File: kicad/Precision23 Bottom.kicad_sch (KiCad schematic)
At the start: 12 parts, among them J396 STANDOFF, J397 STANDOFF, J398 STANDOFF, J399 STANDOFF, J504 Conn_01x06, J507 Conn_01x06, J508 Conn_01x06, J509 Conn_01x02_Pin, J895 USB A Male to Blank

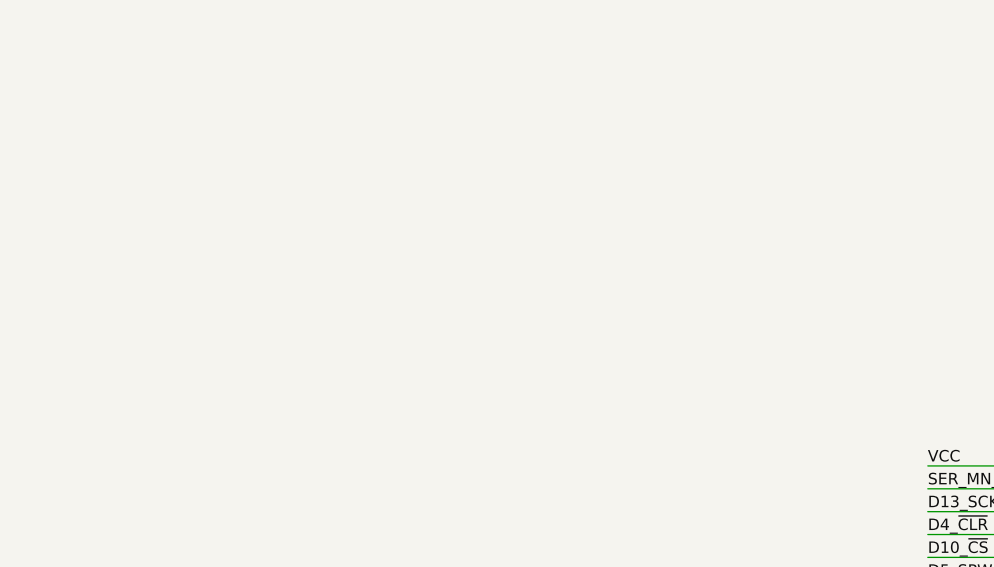
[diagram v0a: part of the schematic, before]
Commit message: Added top and bottom schematics to support refactor of board
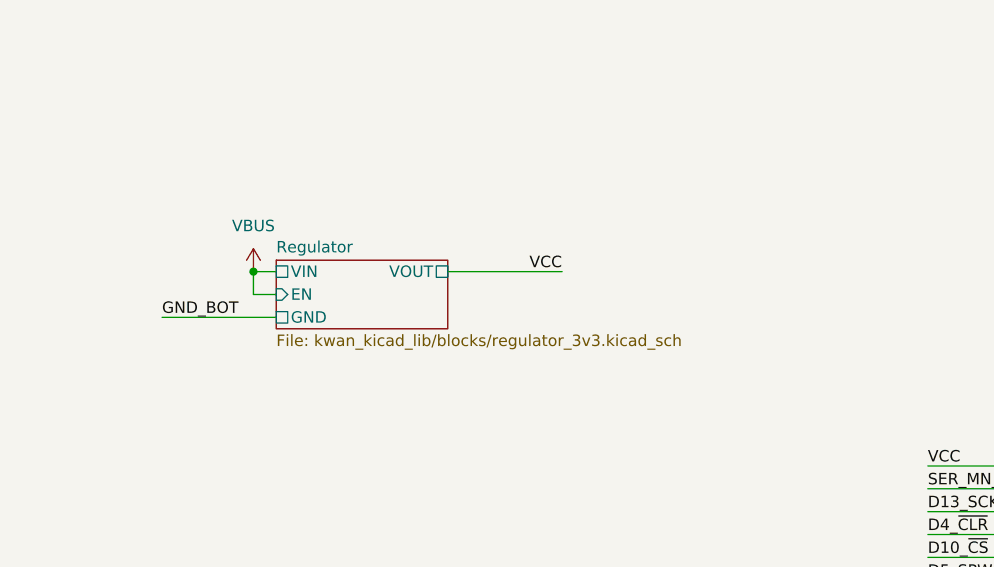
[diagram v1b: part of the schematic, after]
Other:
- added sheet Regulator (kwan_kicad_lib/blocks/regulator_3v3.kicad_sch)
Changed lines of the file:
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@@
   (junction (at 46.99 181.61) (diameter 0) (color 0 0 0 0)
+  )
+  (junction (at 102.87 78.74) (diameter 0) (color 0 0 0 0)
   )
   (junction (at 46.99 179.07) (diameter 0) (color 0 0 0 0)
@@
     (stroke (width 0) (type default))
   )
+  (wire (pts (xy 124.46 78.74) (xy 137.16 78.74))
+    (stroke (width 0) (type default))
+  )
   (wire (pts (xy 46.99 168.91) (xy 57.15 168.91))
     (stroke (width 0) (type default))
@@
     (stroke (width 0) (type default))
   )
+  (wire (pts (xy 105.41 81.28) (xy 102.87 81.28))
+    (stroke (width 0) (type default))
+  )
   (wire (pts (xy 46.99 176.53) (xy 57.15 176.53))
     (stroke (width 0) (type default))
@@
     (stroke (width 0) (type default))
   )
+  (wire (pts (xy 92.71 83.82) (xy 105.41 83.82))
+    (stroke (width 0) (type default))
+  )
   (wire (pts (xy 40.64 41.91) (xy 54.61 41.91))
     (stroke (width 0) (type default))
   )
+  (wire (pts (xy 102.87 78.74) (xy 105.41 78.74))
+    (stroke (width 0) (type default))
+  )
   (wire (pts (xy 34.29 179.07) (xy 46.99 179.07))
     (stroke (width 0) (type default))
@@
   )
   (wire (pts (xy 177.8 127) (xy 190.5 127))
+    (stroke (width 0) (type default))
+  )
+  (wire (pts (xy 102.87 81.28) (xy 102.87 78.74))
     (stroke (width 0) (type default))
   )
@@
     (effects (font (size 1.27 1.27)) (justify left bottom))
   )
+  (label "GND_BOT" (at 92.71 83.82 0) (fields_autoplaced)
+    (effects (font (size 1.27 1.27)) (justify left bottom))
+  )
   (label "GND_BOT" (at 50.8 114.3 180) (fields_autoplaced)
+    (effects (font (size 1.27 1.27)) (justify right bottom))
+  )
+  (label "VCC" (at 137.16 78.74 180) (fields_autoplaced)
     (effects (font (size 1.27 1.27)) (justify right bottom))
   )
@@
     )
   )
+  (symbol (lib_id "power:VBUS") (at 102.87 78.74 0) (unit 1)
+    (in_bom yes) (on_board yes) (dnp no) (fields_autoplaced)
+    (property "Reference" "#PWR0310" (at 102.87 82.55 0)
+      (effects (font (size 1.27 1.27)) hide)
+    )
+    (property "Value" "VBUS" (at 102.87 73.66 0)
+      (effects (font (size 1.27 1.27)))
+    )
+    (property "Footprint" "" (at 102.87 78.74 0)
+      (effects (font (size 1.27 1.27)) hide)
+    )
+    (property "Datasheet" "" (at 102.87 78.74 0)
+      (effects (font (size 1.27 1.27)) hide)
+    )
+    (pin "1")
+    (instances
+      (project "Precision23"
+        (path "/9151f981-b383-4946-8df4-92ef46ef2206"
+          (reference "#PWR0310") (unit 1)
+        )
+        (path "/9151f981-b383-4946-8df4-92ef46ef2206/b9b5a9b9-9a45-4bb4-8a5d-f3809553447a"
+          (reference "#PWR0303") (unit 1)
+        )
+        (path "/9151f981-b383-4946-8df4-92ef46ef2206/9f66be35-2744-413f-8b31-a996047a434b"
+          (reference "#PWR0303") (unit 1)
+        )
+      )
+    )
+  )
   (symbol (lib_id "Connector_Generic:Conn_01x06") (at 59.69 39.37 0) (unit 1)
     (in_bom yes) (on_board yes) (dnp no)
@@
       )
     )
+  )
+  (sheet (at 105.41 77.47) (size 19.05 7.62) (fields_autoplaced)
+    (stroke (width 0.1524) (type solid))
+    (fill (color 0 0 0 0.0000))
+    (property "Sheetname" "Regulator" (at 105.41 76.7584 0)
+      (effects (font (size 1.27 1.27)) (justify left bottom))
+    )
+    (property "Sheetfile" "kwan_kicad_lib/blocks/regulator_3v3.kicad_sch" (at 105.41 85.6746 0)
+      (effects (font (size 1.27 1.27)) (justify left top))
+    )
+    (pin "GND" passive (at 105.41 83.82 180)
+      (effects (font (size 1.27 1.27)) (justify left))
+    )
+    (pin "VIN" passive (at 105.41 78.74 180)
+      (effects (font (size 1.27 1.27)) (justify left))
+    )
+    (pin "EN" input (at 105.41 81.28 180)
+      (effects (font (size 1.27 1.27)) (justify left))
+    )
+    (pin "VOUT" passive (at 124.46 78.74 0)
+      (effects (font (size 1.27 1.27)) (justify right))
+    )
+    (instances
+      (project "Precision23"
+        (path "/9151f981-b383-4946-8df4-92ef46ef2206" (page "6"))
+        (path "/9151f981-b383-4946-8df4-92ef46ef2206/b9b5a9b9-9a45-4bb4-8a5d-f3809553447a" (page "6"))
+        (path "/9151f981-b383-4946-8df4-92ef46ef2206/9f66be35-2744-413f-8b31-a996047a434b" (page "6"))
+      )
+    )

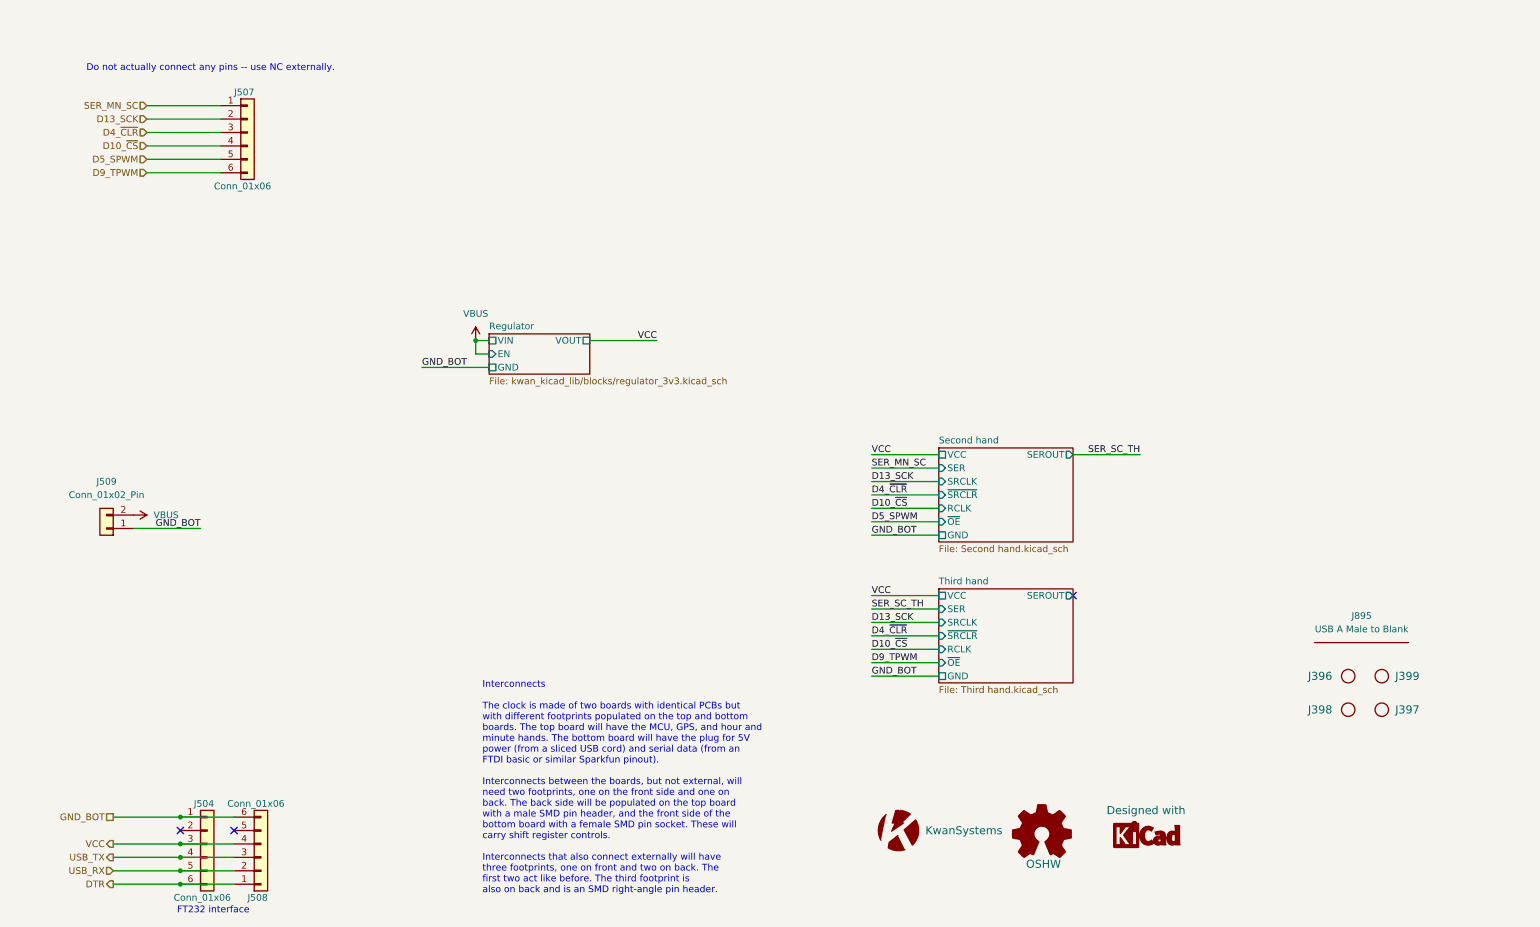
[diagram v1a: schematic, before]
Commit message: Refactored board, put 5V0 on all parts except GPS
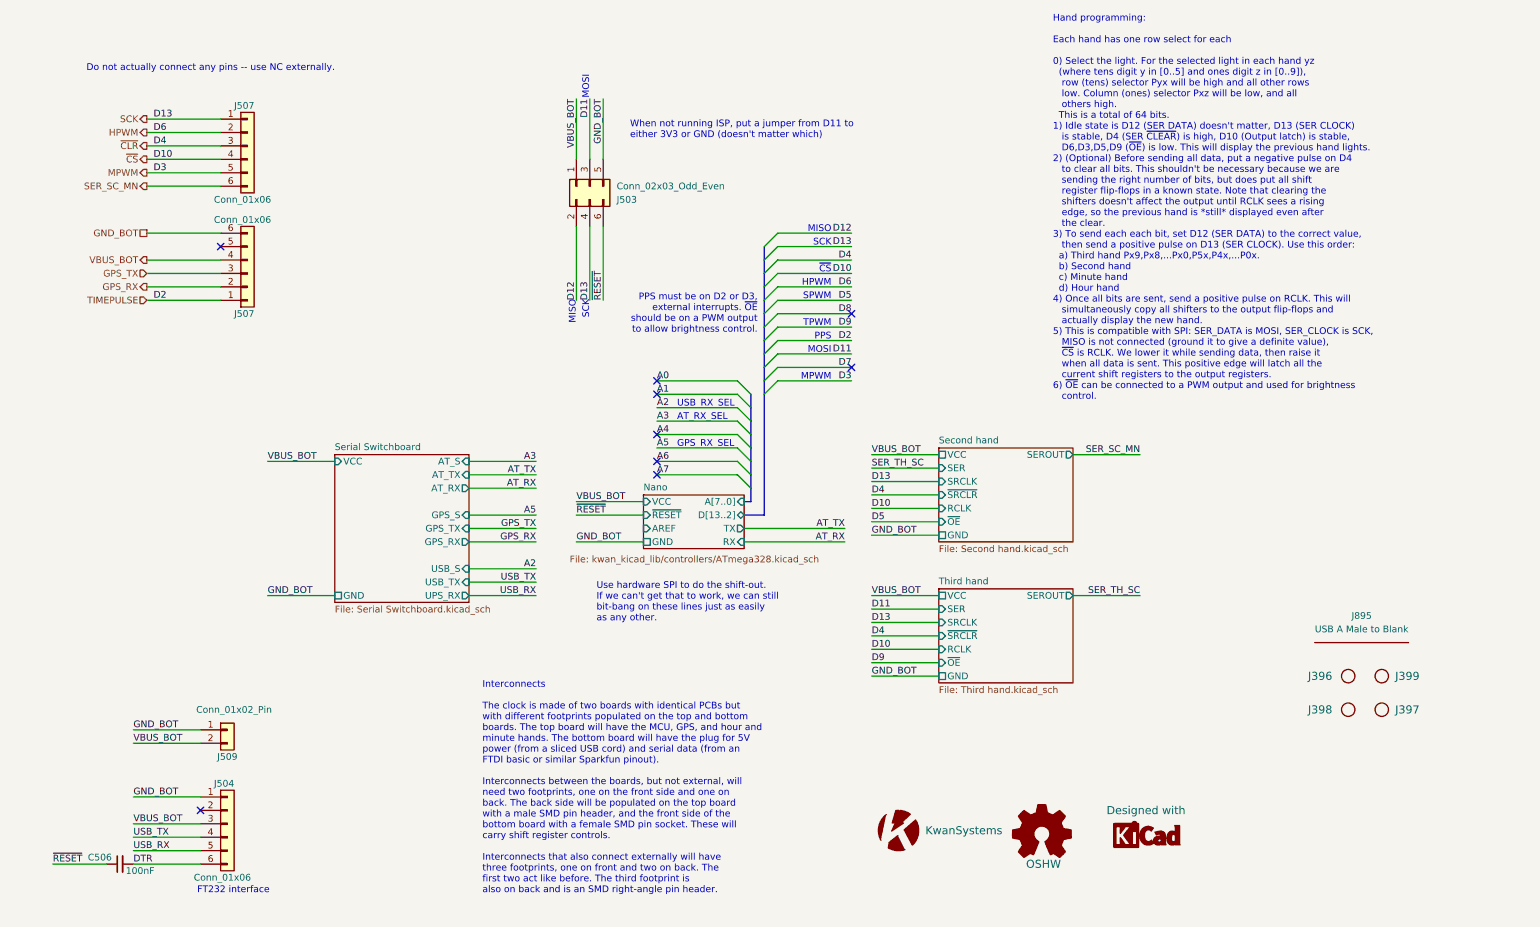
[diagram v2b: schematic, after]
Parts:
- removed J508: Conn_01x06, Connector_PinSocket_2.54mm:PinSocket_1x06_P2.54mm_Vertical_SMD_Pin1Left, symbol Connector_Generic:Conn_01x06
- added C506: 100nF, Capacitor_SMD:C_0603_1608Metric, symbol Device:C_Small
- added J503: Conn_02x03_Odd_Even, Connector_PinSocket_2.54mm:PinSocket_2x03_P2.54mm_Vertical_SMD, symbol Connector_Generic:Conn_02x03_Odd_Even
- added J507: Conn_01x06, Connector_PinSocket_2.54mm:PinSocket_1x06_P2.54mm_Vertical_SMD_Pin1Left, symbol Connector_Generic:Conn_01x06
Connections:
- net VCC is gone; now on net VBUS_BOT: J504.3 (Pin_3)
- net DTR: now also C506.2
- net GND_BOT: now also J503.5 (Pin_5), J507.6 (Pin_6)
- net D10_~{CS} renamed ~{CS}
- net D13_SCK renamed HPWM
- net D4_~{CLR} renamed ~{CLR}
- net D5_SPWM renamed MPWM
- net D9_TPWM renamed SER_SC_MN
- net SER_MN_SC renamed SCK
- net SCK: now also J503.4 (Pin_4)
- net VBUS renamed VBUS_BOT
- net VBUS_BOT: now also J503.1 (Pin_1), J507.4 (Pin_4)
- new net D11: J503.3 (Pin_3)
- new net D12: J503.2 (Pin_2)
- new net GPS_RX: J507.2 (Pin_2)
- new net GPS_TX: J507.3 (Pin_3)
- new net TIMEPULSE: J507.1 (Pin_1)
- new net ~{RESET}: C506.1, J503.6 (Pin_6)
- no-connect marks 3 -> 9
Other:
- removed sheet Regulator
- added sheet Nano (kwan_kicad_lib/controllers/ATmega328.kicad_sch)
- added sheet Serial Switchboard (Serial Switchboard.kicad_sch)
- note added: "AT_RX_SEL"
- note added: "GPS_RX_SEL"
- note added: "HPWM"
- note added: "Hand programming: Each hand has one row select for each 0) Select the light. For the selected light in each hand yz (where tens digit y in [0..5] and ones digit z in [0..9]), row (tens) selector Pyx will be high and all other rows low. Column (ones) selector Pxz will be low, and all others high. This is a total of 64 bits. 1) Idle state is D12 (SER DATA) doesn't matter, D13 (SER CLOCK) is stable,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"
- note added: "MISO"
- note added: "MOSI"
- note added: "MPWM"
- note added: "PPS"
- note added: "PPS must be on D2 or D3, external interrupts. ~{OE} should be on a PWM output to allow brightness control."
- note added: "SCK"
- note added: "SPWM"
- note added: "TPWM"
- note added: "USB_RX_SEL"
- note added: "Use hardware SPI to do the shift-out. If we can't get that to work, we can still bit-bang on these lines just as easily as any other."
- note added: "When not running ISP, put a jumper from D11 to either 3V3 or GND (doesn't matter which)"
- note added: "~{CS}"
- moved on the sheet: J504, J507, J509
